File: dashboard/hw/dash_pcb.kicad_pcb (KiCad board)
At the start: 2 copper layers, 180 x 65 mm, 35 parts, among them J1 LCD, J2 DEBUG, J3 LCD_BL, J4 CAR, U1 LPC11C24FBD48, U2 TPS62175, U3 TLV70233_SOT23-5, Y1 12MHz

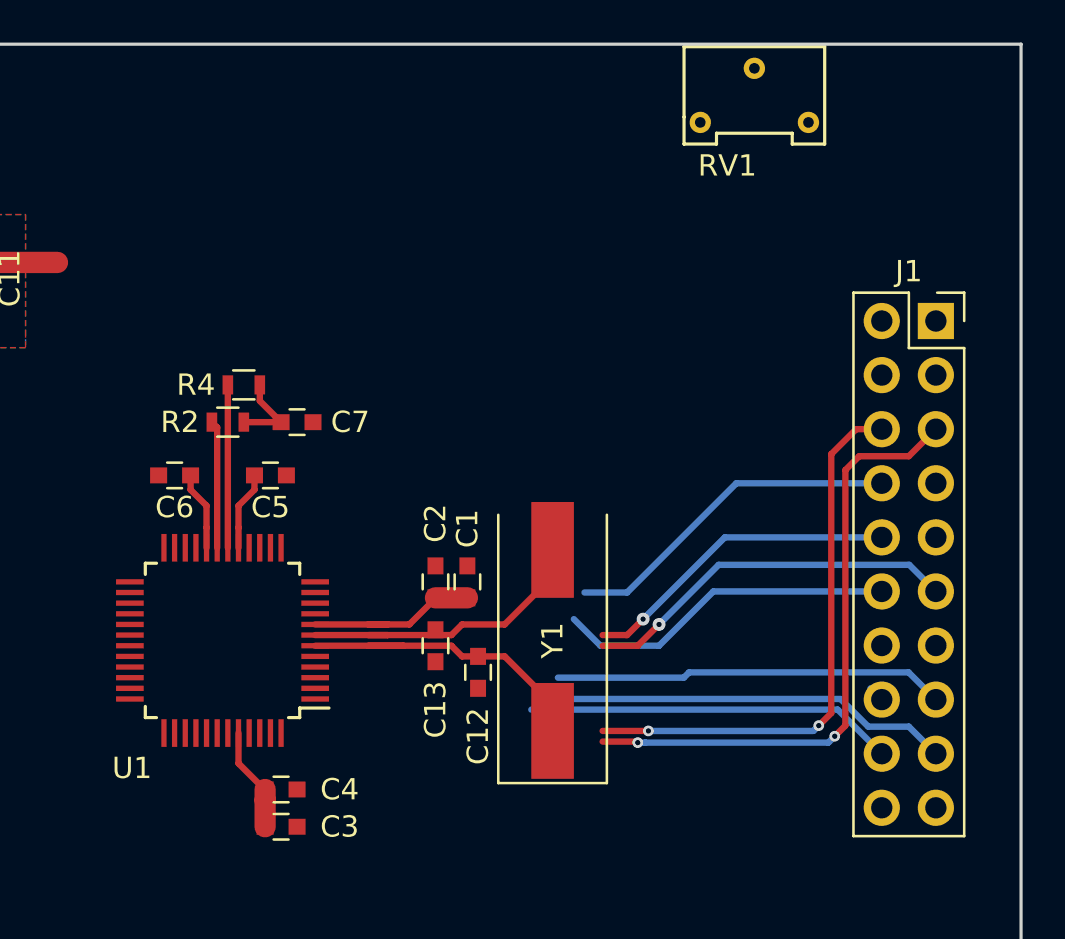
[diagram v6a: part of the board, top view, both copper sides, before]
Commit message: route out lcd connector
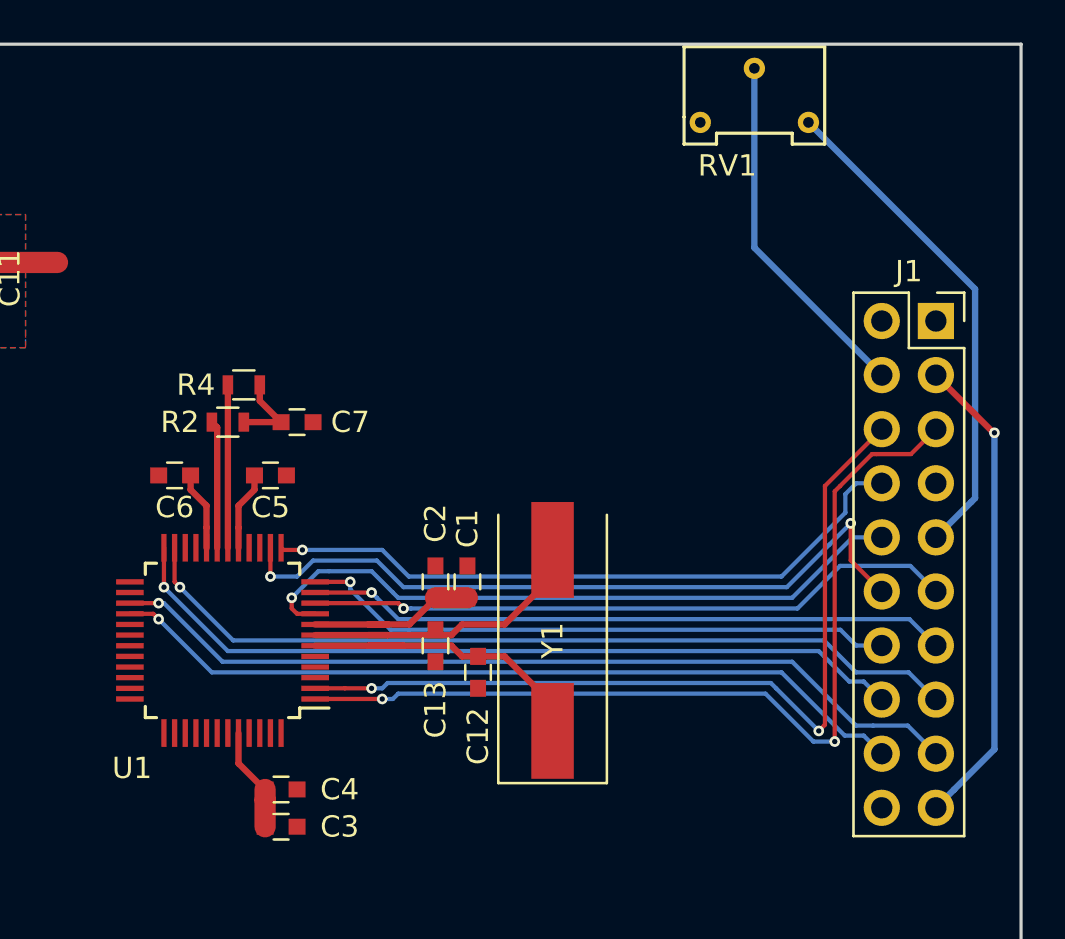
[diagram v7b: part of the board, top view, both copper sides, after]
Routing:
- net /LCD_DB5: track 0.75 -> 37.7 mm, vias 0 -> 1
- net /LCD_DB2: track 0.00 -> 30.2 mm, vias 0 -> 1
- net /LCD_DB3: track 0.00 -> 28.1 mm, vias 0 -> 1
- net /LCD_VEE: track 0.00 -> 23.5 mm
- net +3V3: track 23.5 -> 46.1 mm, vias 0 -> 1
- net /LCD_DB4: track 18.4 -> 39.6 mm, vias 0 -> 1
- net /LCD_DB6: track 19.6 -> 40.8 mm, vias 0 -> 1
- net /LCD_DB7: track 17.3 -> 38.0 mm, vias 0 -> 1
- net /LCD_DB1: track 16.0 -> 34.5 mm, vias 0 -> 2
- net /LCD_V0: track 0.00 -> 16.9 mm
- net /LCD_~RST: track 15.0 -> 31.6 mm
- net /LCD_C/~D: track 16.1 -> 31.1 mm, vias 0 -> 1
- net /LCD_~RD: track 26.1 -> 40.1 mm
- net /LCD_~WR: track 29.6 -> 43.1 mm
- net /LCD_DB0: track 17.7 -> 30.6 mm

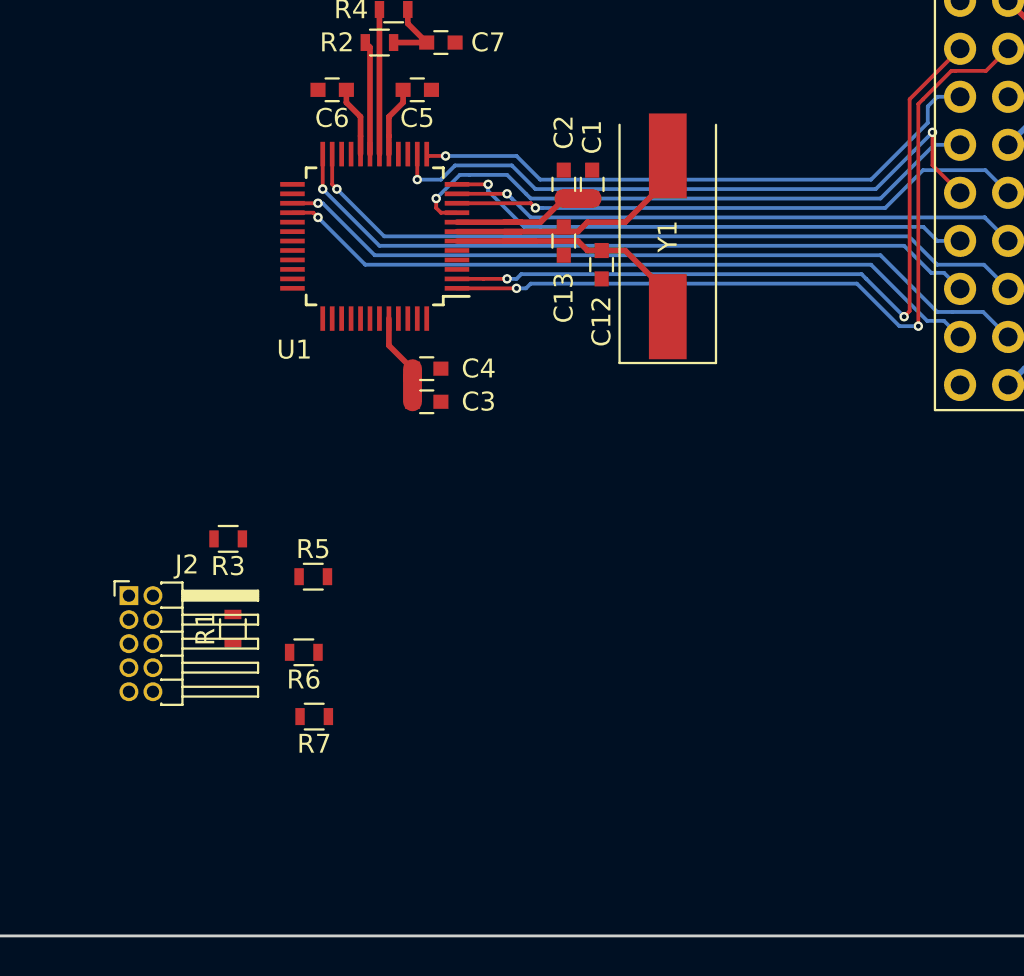
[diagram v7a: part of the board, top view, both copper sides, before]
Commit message: route debug connector
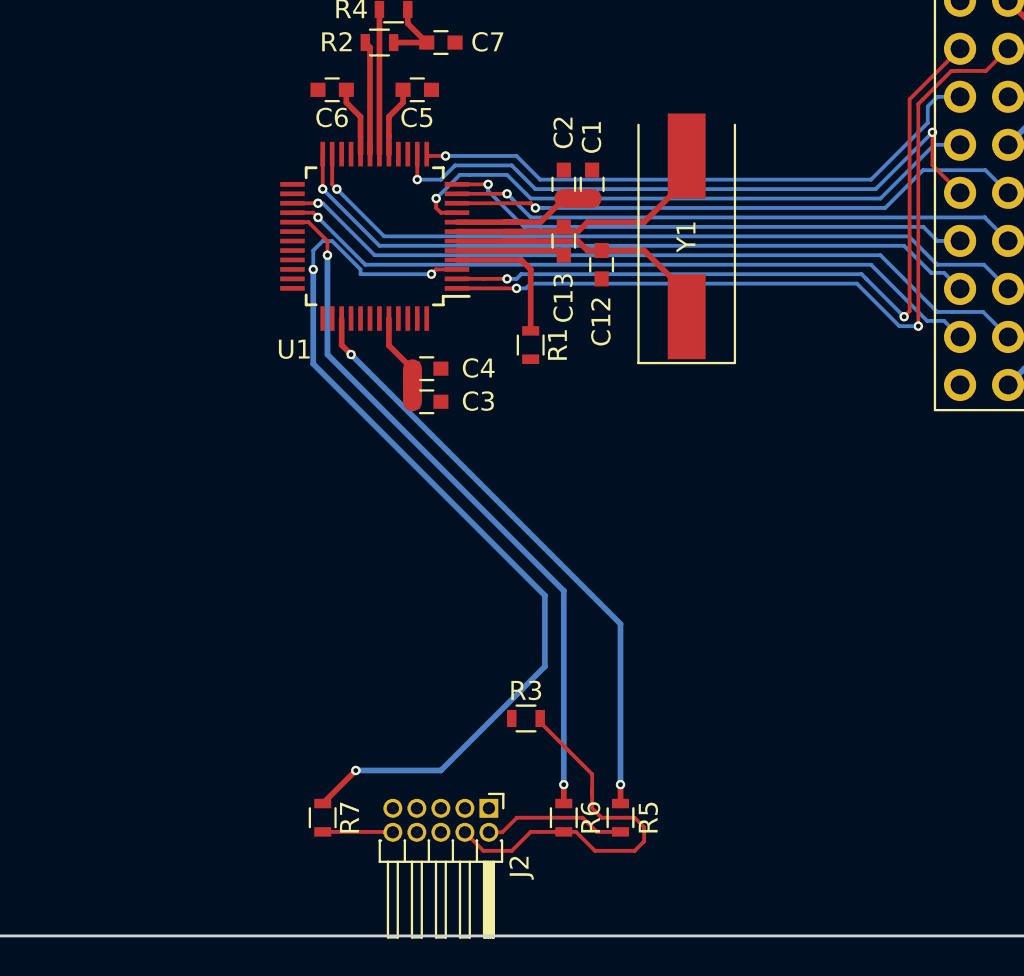
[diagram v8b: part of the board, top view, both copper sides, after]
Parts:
- moved J2 22.1 mm to (233.5, 113.2), turned to 270 degrees
- moved R1 21.8 mm to (235.8, 88.8), turned to 270 degrees
- moved R5 20.7 mm to (240.5, 113.8), turned to 90 degrees
- moved R3 18.4 mm to (235.5, 108.5), turned to 0 degrees
- moved R6 16.3 mm to (237.5, 113.8), turned to 270 degrees
- moved R7 5.37 mm to (224.8, 113.8), turned to 270 degrees
- moved Y1 1.00 mm to (244.0, 83.0)
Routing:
- net /5VPG: track 10.9 -> 61.5 mm, vias 2 -> 5
- net /SWCLK: track 0.00 -> 37.2 mm, vias 0 -> 2
- net /SWDIO: track 0.00 -> 31.8 mm, vias 0 -> 2
- net Net-(J2-Pad4): track 0.00 -> 21.0 mm
- net Net-(J2-Pad2): track 0.00 -> 7.59 mm
- net Net-(R1-Pad1): track 0.00 -> 7.36 mm
- net GND: track 11.2 -> 16.9 mm
- net Net-(J2-Pad10): track 0.00 -> 3.72 mm
- net /XTALOUT: track 14.4 -> 15.4 mm
- net /XTALIN: track 14.9 -> 15.9 mm
